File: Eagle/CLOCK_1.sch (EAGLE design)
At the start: 24 parts, among them IC1 DS1307, IC2 HKW581, J1 AUDIO_JACK_3.5MM_PTH, U1 328P, U2 SN74HC595N, U3 SN74HC595N, U4 SN74HC595N, U5 SN74HC595N

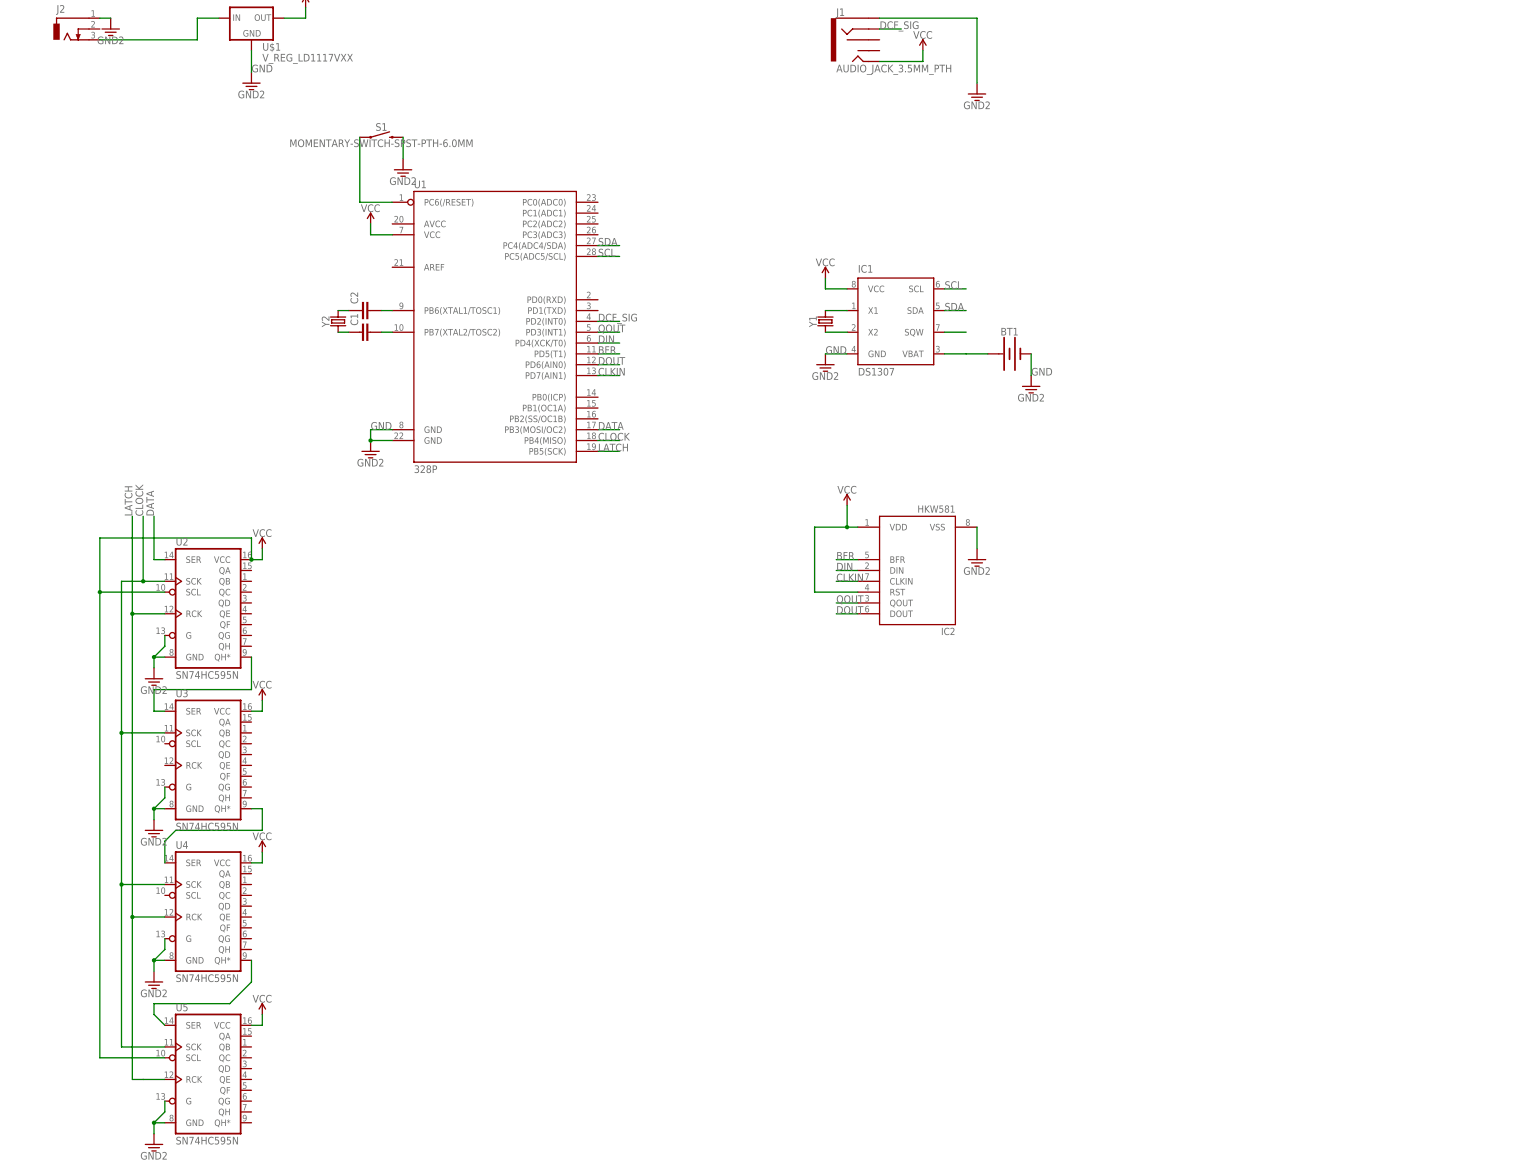
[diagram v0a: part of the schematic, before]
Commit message: ADD SERIALIN/PARALELLOUT 74HC165 ADD LCD
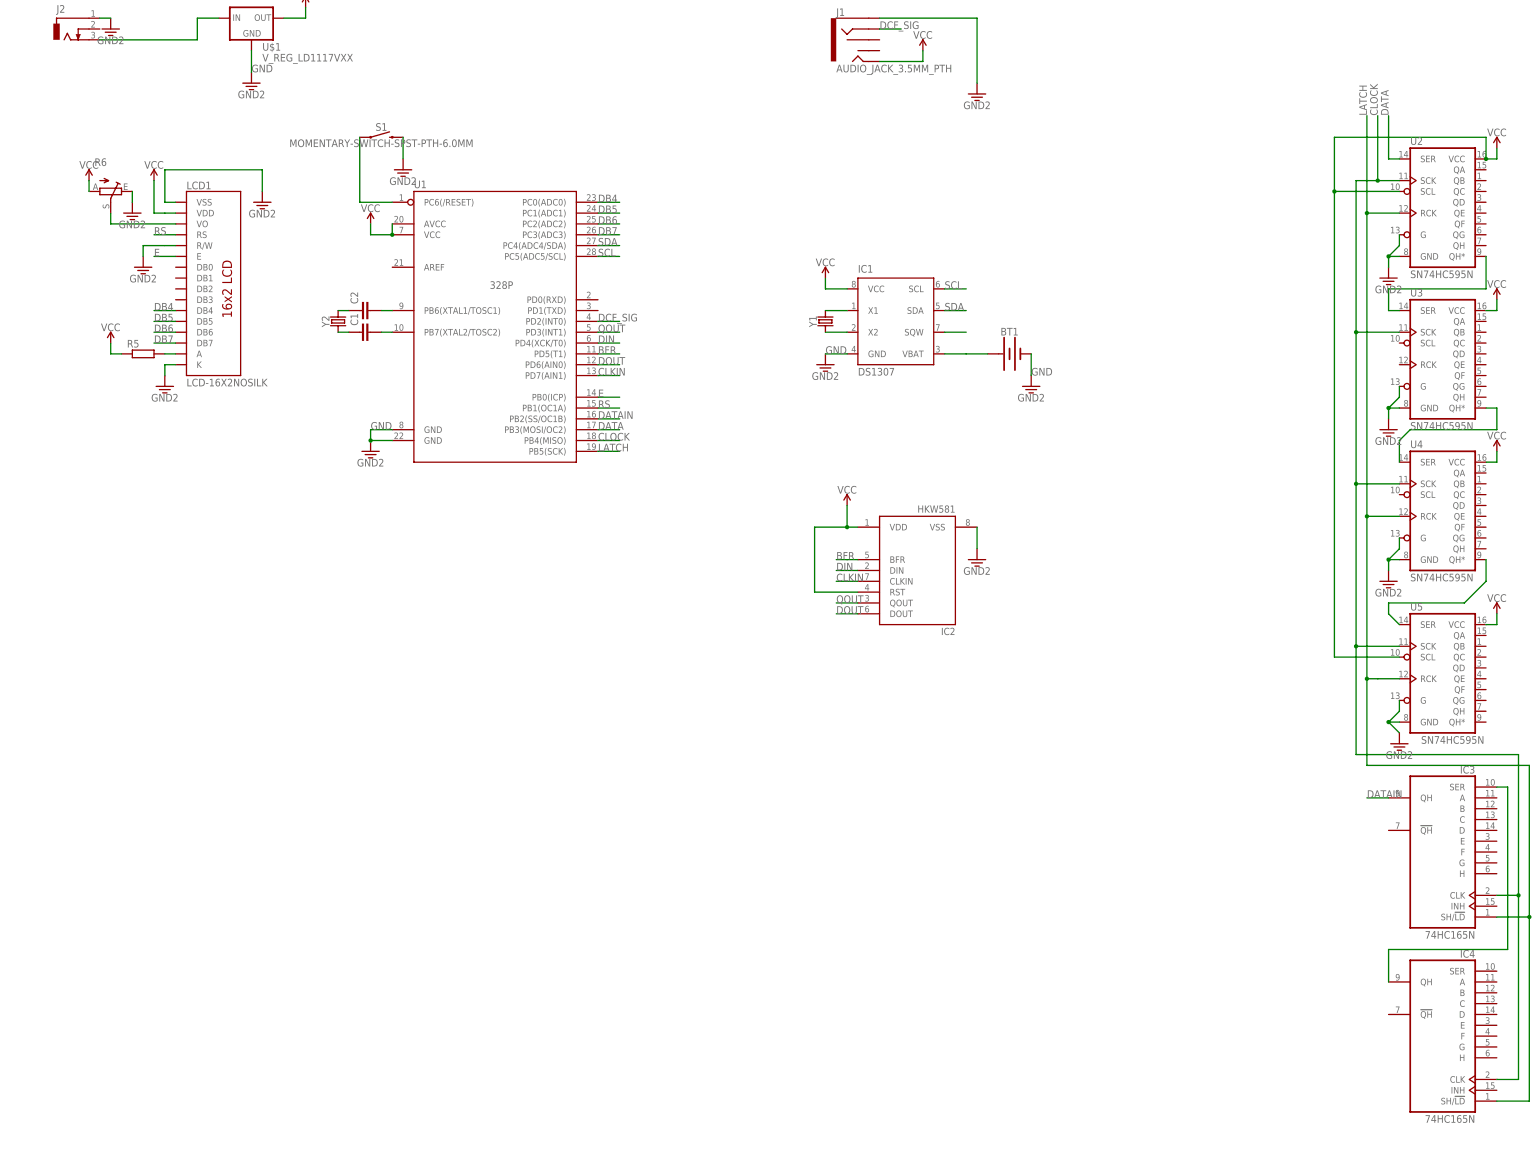
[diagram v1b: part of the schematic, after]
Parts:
- added IC3, IC4: 74HC165N, 74xx-eu:74HC165N
- added LCD1: LCD-16X2NOSILK, SparkFun-Displays:LCD-16X2NOSILK
- added R5: (no value), rcl:R-EU_0207/10
- added R6: (no value), pot:TRIM_EU-B25U
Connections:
- new net DATAIN: IC3A.QH, U1.PB2(SS/OC1B)
- new net DB4: LCD1.DB4, U1.PC0(ADC0)
- new net DB5: LCD1.DB5, U1.PC1(ADC1)
- new net DB6: LCD1.DB6, U1.PC2(ADC2)
- new net DB7: LCD1.DB7, U1.PC3(ADC3)
- new net E: LCD1.E, U1.PB0(ICP)
- new net N$21: LCD1.A, R5.2
- new net N$32: LCD1.VO, R6.S
- new net N$4: IC3A.SER, IC4A.QH
- new net RS: LCD1.RS, U1.PB1(OC1A)
- net CLOCK: now also IC3A.CLK, IC4A.CLK
- net GND: now also LCD1.K, LCD1.R/W, LCD1.VSS, R6.E
- net LATCH: now also IC3A.SH/!LD, IC4A.SH/!LD
- net VCC: now also LCD1.VDD, R5.1, R6.A, U1.AVCC
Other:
- moved on the sheet: U2, U3, U4, U5

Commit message: ADD pushbtton ADD 7-Segment ADD FTDI ADD BUZZER
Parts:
- added C10, C11, C12, C13, C14, C15, C16, C17, C3, C31, C32, C4, C5, C6, C7, C8, C9: 10u, rcl:CPOL-EUE5-8.5
- added C18, C19, C20, C21, C22, C23, C24, C25, C26, C27, C28, C29, C30: 100n, rcl:C-EU025-025X050
- added DIS1, DIS10, DIS11, DIS12, DIS13, DIS14, DIS2, DIS3, DIS4, DIS5, DIS6, DIS7, DIS8, DIS9: HD-H103, display-hp:HD-H103
- added IC5: NE555, st-microelectronics:NE555
- added JP1: (no value), pinhead:PINHD-1X4
- added LED10, LED11, LED5, LED6, LED7, LED8, LED9: (no value), led:LED5MM
- added LS1: BUZZER-PTH, SparkFun-Electromechanical:BUZZER-PTH
- added R10, R11, R12, R13, R14, R15, R16, R17, R18, R19, R20, R21, R22, R25, R7, R8, R9: 10k, resistor:R-EU_0207/10
- added R100, R101, R102, R103, R104, R105, R106, R107, R108, R109, R110, R111, R112, R113, R114, R115, R116, R117, R118, R119, R120, R121, R122, R123, R124, R125, R126, R127, R128, R129, R130, R131, R132, R133, R134, R135, R136, R137, R138, R139, R140, R141, R142, R143, R144, R33, R34, R35, R36, R37, R38, R39, R40, R41, R42, R43, R44, R45, R46, R47, R48, R49, R50, R51, R52, R53, R54, R55, R56, R57, R58, R59, R60, R61, R62, R63, R64, R65, R66, R67, R68, R69, R70, R71, R72, R73, R74, R75, R76, R77, R78, R79, R80, R81, R82, R83, R84, R85, R86, R87, R88, R89, R90, R91, R92, R93, R94, R95, R96, R97, R98, R99: 330, rcl:R-EU_0207/10
- added R23, R24: 100, rcl:R-EU_0207/10
- added R26, R27, R28, R29, R30, R31, R32: 220, rcl:R-EU_0207/10
- added S10, S11, S12, S13, S14, S15, S16, S17, S2, S3, S4, S5, S6, S7, S8, S9: MOMENTARY-SWITCH-SPST-PTH-6.0MM, SparkFun-Switches:MOMENTARY-SWITCH-SPST-PTH-6.0MM
- R1, R2, R3, R4, R5: value (none) -> 220
- R6: value (none) -> 10k
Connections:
- removed net N$18: U4.QH*, U5.SER
- new net A: R103.2, R111.2, R119.2, R127.2, R135.2, R143.2, R39.2, R47.2, R55.2, R63.2, R71.2, R79.2, R87.2, R95.2, U2.QA
- new net B: R102.2, R110.2, R118.2, R126.2, R134.2, R142.2, R38.2, R46.2, R54.2, R62.2, R70.2, R78.2, R86.2, R94.2, U2.QB
- new net BUZZ: IC5./RES, R25.2, U4.QG
- new net C: R101.2, R109.2, R117.2, R125.2, R133.2, R141.2, R37.2, R45.2, R53.2, R61.2, R69.2, R77.2, R85.2, R93.2, U2.QC
- new net D: R100.2, R108.2, R116.2, R124.2, R132.2, R140.2, R36.2, R44.2, R52.2, R60.2, R68.2, R76.2, R84.2, R92.2, U2.QD
- new net D0: DIS7.CC, DIS7.CC@1, U3.QG
- new net D1: DIS8.CC, DIS8.CC@1, U3.QH
- new net DP: R104.1, R112.1, R120.1, R128.1, R136.1, R144.1, R40.1, R48.1, R56.1, R64.1, R72.1, R80.1, R88.1, R96.1, U2.QH
- new net F: R106.2, R114.2, R122.2, R130.2, R138.2, R34.2, R42.2, R50.2, R58.2, R66.2, R74.2, R82.2, R90.2, R98.2, U2.QF
- new net G: R105.2, R113.2, R121.2, R129.2, R137.2, R33.2, R41.2, R49.2, R57.2, R65.2, R73.2, R81.2, R89.2, R97.2, U2.QG
- new net H0: DIS1.CC, DIS1.CC@1, U3.QA
- new net H1: DIS2.CC, DIS2.CC@1, U3.QB
- new net M0: DIS9.CC, DIS9.CC@1, U4.QA
- new net M1: DIS10.CC, DIS10.CC@1, U4.QB
- new net MI0: DIS3.CC, DIS3.CC@1, U3.QC
- new net MI1: DIS4.CC, DIS4.CC@1, U3.QD
- new net N$101: DIS6.G, R73.1
- new net N$102: DIS6.F, R74.1
- new net N$103: DIS6.E, R75.1
- new net N$104: DIS6.D, R76.1
- new net N$105: DIS6.C, R77.1
- new net N$106: DIS6.B, R78.1
- new net N$107: DIS6.A, R79.1
- new net N$108: DIS6.DP, R80.2
- new net N$110: DIS7.G, R81.1
- new net N$111: DIS7.F, R82.1
- new net N$112: DIS7.E, R83.1
- new net N$113: DIS7.D, R84.1
- new net N$114: DIS7.C, R85.1
- new net N$115: DIS7.B, R86.1
- new net N$116: DIS7.A, R87.1
- new net N$117: DIS7.DP, R88.2
- new net N$119: DIS8.G, R89.1
- new net N$120: DIS8.F, R90.1
- new net N$121: DIS8.E, R91.1
- new net N$122: DIS8.D, R92.1
- new net N$123: DIS8.C, R93.1
- new net N$124: DIS8.B, R94.1
- new net N$125: DIS8.A, R95.1
- new net N$126: DIS8.DP, R96.2
- new net N$128: DIS9.G, R97.1
- new net N$129: DIS9.F, R98.1
- new net N$130: DIS9.E, R99.1
- new net N$131: DIS9.D, R100.1
- new net N$132: DIS9.C, R101.1
- new net N$133: DIS9.B, R102.1
- new net N$134: DIS9.A, R103.1
- new net N$135: DIS9.DP, R104.2
- new net N$137: DIS10.G, R105.1
- new net N$138: DIS10.F, R106.1
- new net N$139: DIS10.E, R107.1
- new net N$140: DIS10.D, R108.1
- new net N$141: DIS10.C, R109.1
- new net N$142: DIS10.B, R110.1
- new net N$143: DIS10.A, R111.1
- new net N$144: DIS10.DP, R112.2
- new net N$146: DIS11.G, R113.1
- new net N$147: DIS11.F, R114.1
- new net N$148: DIS11.E, R115.1
- new net N$149: DIS11.D, R116.1
- new net N$150: DIS11.C, R117.1
- new net N$151: DIS11.B, R118.1
- new net N$152: DIS11.A, R119.1
- new net N$153: DIS11.DP, R120.2
- new net N$155: DIS12.G, R121.1
- new net N$156: DIS12.F, R122.1
- new net N$157: DIS12.E, R123.1
- new net N$158: DIS12.D, R124.1
- new net N$159: DIS12.C, R125.1
- new net N$160: DIS12.B, R126.1
- new net N$161: DIS12.A, R127.1
- new net N$162: DIS12.DP, R128.2
- new net N$164: DIS13.G, R129.1
- new net N$165: DIS13.F, R130.1
- new net N$166: DIS13.E, R131.1
- new net N$167: DIS13.D, R132.1
- new net N$168: DIS13.C, R133.1
- new net N$169: DIS13.B, R134.1
- new net N$170: DIS13.A, R135.1
- new net N$171: DIS13.DP, R136.2
- new net N$173: DIS14.G, R137.1
- new net N$174: DIS14.F, R138.1
- new net N$175: DIS14.E, R139.1
- new net N$176: DIS14.D, R140.1
- new net N$177: DIS14.C, R141.1
- new net N$178: DIS14.B, R142.1
- new net N$179: DIS14.A, R143.1
- new net N$180: DIS14.DP, R144.2
- new net N$19: IC3A.A, R7.1, S2.1
- new net N$197: U4.QH
- new net N$20: IC3A.B, R8.1, S3.1
- new net N$22: IC3A.C, R9.1, S4.1
- new net N$23: IC3A.D, R10.1, S5.1
- new net N$24: IC3A.E, R11.1, S6.1
- new net N$25: IC3A.F, R12.1, S7.1
- new net N$26: IC3A.G, R13.1, S8.1
- new net N$27: IC3A.H, R14.1, S9.1
- new net N$28: IC4A.A, R15.1, S10.1
- new net N$29: IC4A.B, R16.1, S11.1
- new net N$30: IC4A.C, R17.1, S12.1
- new net N$31: IC4A.D, R18.1, S13.1
- new net N$33: IC4A.E, R19.1, S14.1
- new net N$34: IC4A.F, R20.1, S15.1
- new net N$35: IC4A.G, R21.1, S16.1
- new net N$36: IC4A.H, R22.1, S17.1
- new net N$37: IC5.DIS, R23.1, R24.2
- new net N$38: C31.+, IC5.TRE, IC5.TRI, R24.1
- new net N$39: C32.+, IC5.CON
- new net N$41: R26.2, U5.QA
- new net N$42: IC5.OUT, LS1.1
- new net N$43: R27.2, U5.QB
- new net N$44: R28.2, U5.QC
- new net N$45: R29.2, U5.QD
- new net N$46: R30.2, U5.QE
- new net N$47: R31.2, U5.QF
- new net N$48: R32.2, U5.QG
- new net N$49: LED5.A, R26.1
- new net N$50: LED6.A, R27.1
- new net N$51: LED7.A, R28.1
- new net N$52: LED8.A, R29.1
- new net N$53: LED9.A, R30.1
- new net N$54: LED10.A, R31.1
- new net N$55: LED11.A, R32.1
- new net N$57: DIS2.G, R41.1
- new net N$58: DIS2.F, R42.1
- new net N$59: DIS2.E, R43.1
- new net N$60: DIS2.D, R44.1
- new net N$61: DIS2.C, R45.1
- new net N$62: DIS2.B, R46.1
- new net N$63: DIS2.A, R47.1
- new net N$64: DIS1.G, R33.1
- new net N$65: DIS1.F, R34.1
- new net N$66: DIS1.E, R35.1
- new net N$67: DIS1.D, R36.1
- new net N$68: DIS1.C, R37.1
- new net N$69: DIS1.B, R38.1
- new net N$70: DIS1.A, R39.1
- new net N$71: DIS2.DP, R48.2
- new net N$73: DIS3.G, R49.1
- new net N$74: DIS3.F, R50.1
- new net N$75: DIS3.E, R51.1
- new net N$76: DIS3.D, R52.1
- new net N$77: DIS3.C, R53.1
- new net N$78: DIS1.DP, R40.2
- new net N$79: DIS3.B, R54.1
- new net N$80: DIS3.A, R55.1
- new net N$81: DIS3.DP, R56.2
- new net N$83: DIS4.G, R57.1
- new net N$84: DIS4.F, R58.1
- new net N$85: DIS4.E, R59.1
- new net N$86: DIS4.D, R60.1
- new net N$87: DIS4.C, R61.1
- new net N$88: DIS4.B, R62.1
- new net N$89: DIS4.A, R63.1
- new net N$90: DIS4.DP, R64.2
- new net N$92: DIS5.G, R65.1
- new net N$93: DIS5.F, R66.1
- new net N$94: DIS5.E, R67.1
- new net N$95: DIS5.D, R68.1
- new net N$96: DIS5.C, R69.1
- new net N$97: DIS5.B, R70.1
- new net N$98: DIS5.A, R71.1
- new net N$99: DIS5.DP, R72.2
- new net RX: JP1.3, U1.PD0(RXD)
- new net S0: DIS5.CC, DIS5.CC@1, U3.QE
- new net S1: DIS6.CC, DIS6.CC@1, U3.QF
- new net TX: JP1.4, U1.PD1(TXD)
- new net W: R107.2, R115.2, R123.2, R131.2, R139.2, R35.2, R43.2, R51.2, R59.2, R67.2, R75.2, R83.2, R91.2, R99.2, U2.QE
- new net Y0: DIS11.CC, DIS11.CC@1, U4.QC
- new net Y1: DIS12.CC, DIS12.CC@1, U4.QD
- new net Y2: DIS13.CC, DIS13.CC@1, U4.QE
- new net Y3: DIS14.CC, DIS14.CC@1, U4.QF
- net GND: now also C10.-, C11.-, C12.-, C13.-, C14.-, C15.-, C16.-, C17.-, C18.1, C19.1, C20.1, C21.1, C22.1, C23.1, C24.1, C25.1, C26.1, C27.1, C28.1, C29.1, C3.-, C30.1, C31.-, C32.-, C4.-, C5.-, C6.-, C7.-, C8.-, C9.-, IC5.GND, JP1.1, LED10.C, LED11.C, LED5.C, LED6.C, LED7.C, LED8.C, LED9.C, LS1.2, R10.2, R11.2, R12.2, R13.2, R14.2, R15.2, R16.2, R17.2, R18.2, R19.2, R20.2, R21.2, R22.2, R25.1, R7.2, R8.2, R9.2
- net N$1: now also C3.+
- net VCC: now also C10.+, C11.+, C12.+, C13.+, C14.+, C15.+, C16.+, C17.+, C18.2, C19.2, C20.2, C21.2, C22.2, C23.2, C24.2, C25.2, C26.2, C27.2, C28.2, C29.2, C30.2, C4.+, C5.+, C6.+, C7.+, C8.+, C9.+, IC5.VCC+, JP1.2, R23.2, S10.2, S11.2, S12.2, S13.2, S14.2, S15.2, S16.2, S17.2, S2.2, S3.2, S4.2, S5.2, S6.2, S7.2, S8.2, S9.2, U1.AREF
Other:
- moved on the sheet: BT1, C1, C2, IC1, IC2, IC3, IC4, J1, J2, LCD1, LED1, LED2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
